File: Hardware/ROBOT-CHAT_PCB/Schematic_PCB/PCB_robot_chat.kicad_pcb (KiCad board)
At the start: 4 copper layers, 64.5 x 57 mm, 95 parts, among them J1 Conn_01x04, J201 Conn_ST_STDC14, J3 Conn_01x02, J4 Conn_01x02, J5 Conn_01x02, J501 Conn_01x04, J502 Conn_01x04, J503 Conn_01x04, J504 Conn_01x04, J6 Conn_01x02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

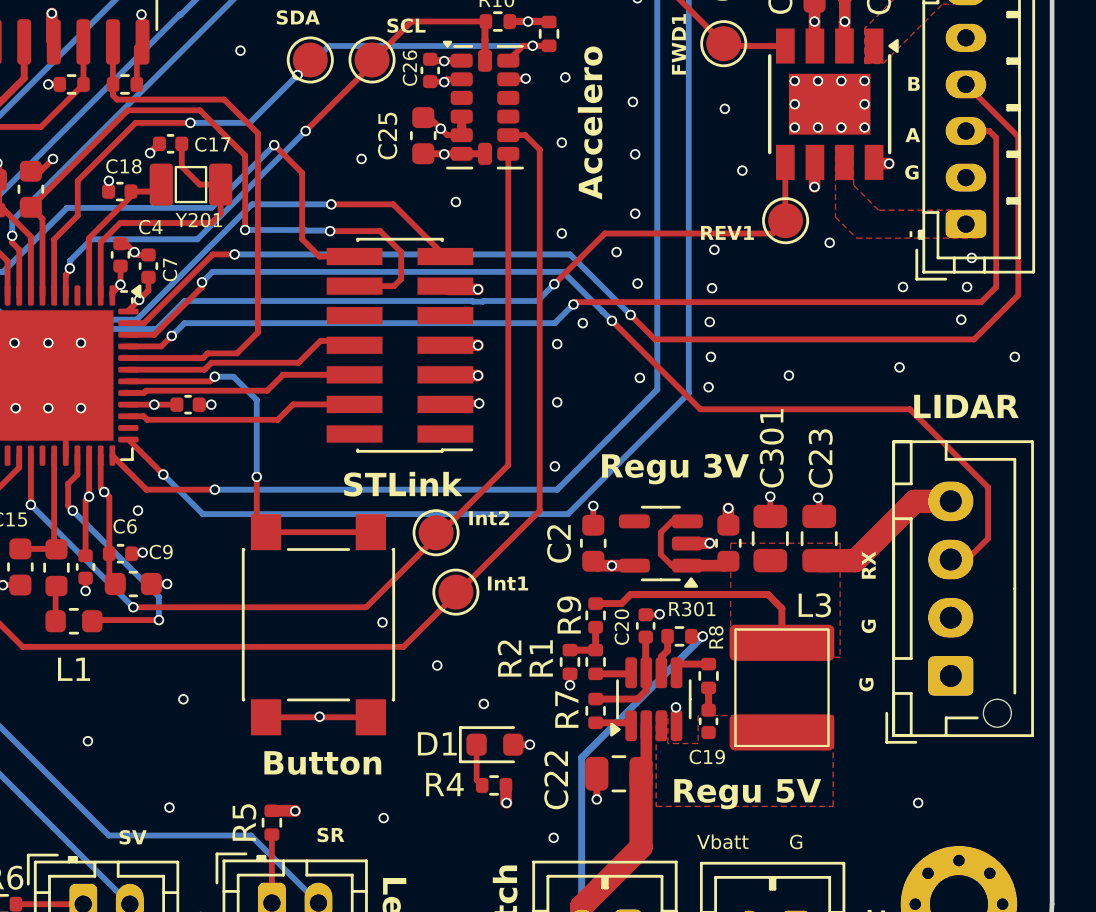
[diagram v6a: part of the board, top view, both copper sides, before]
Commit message: Modified pin M_control for the Lidar, PCV version 7
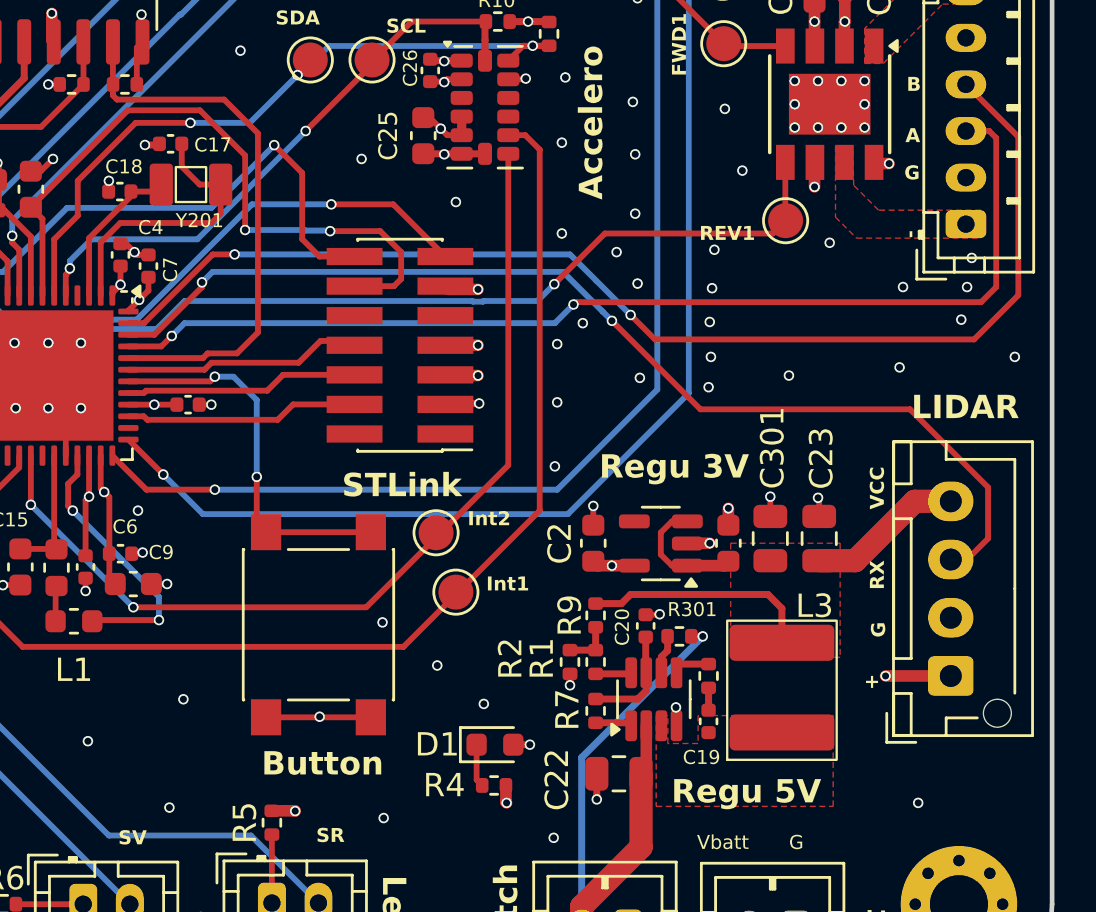
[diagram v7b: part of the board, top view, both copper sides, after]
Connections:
- J1 pad 1: GND -> +3.3V
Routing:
- net +3.3V: track 47.1 -> 49.9 mm, vias 23 -> 24
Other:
- board text added: "VCC"
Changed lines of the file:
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@@
 		(attr smd)
 		(fp_rect
-			(start -2.425 1.5)
-			(end 2.575 5.5)
+			(start -3.025 1.15)
+			(end 2.95 5.85)
 			(stroke
 				(width 0.1)
@@
 			(remove_unused_layers no)
 			(roundrect_rratio 0.147059)
-			(net 2 "GND")
+			(net 3 "+3.3V")
 			(pinfunction "Pin_1")
 			(pintype "passive")
@@
 		(tags "resistor")
 		(property "Reference" "R8"
-			(at -1.65 -0.35 90)
+			(at -1.35 -0.3 90)
 			(layer "F.SilkS")
+			(hide yes)
 			(effects
 				(font
@@
 		(tags "capacitor")
 		(property "Reference" "C19"
-			(at 1.55 0.05 180)
+			(at 1.55 0.3 180)
 			(layer "F.SilkS")
 			(effects
@@
 		)
 	)
-	(gr_text "G"
-		(at 158.4 72.9 90)
-		(layer "F.SilkS")
-		(effects
-			(font
-				(size 0.6 0.6)
-				(thickness 0.15)
-				(bold yes)
-			)
-			(justify left bottom)
-		)
-	)
 	(gr_text "B"
 		(at 159.75 47.15 0)
@@
 		)
 	)
+	(gr_text "VCC"
+		(at 158.85 65.05 90)
+		(layer "F.SilkS")
+		(effects
+			(font
+				(size 0.6 0.6)
+				(thickness 0.15)
+				(bold yes)
+			)
+			(justify left bottom)
+		)
+	)
 	(gr_text "TOF2"
 		(at 116.3 40.2 90)
@@
 	)
 	(gr_text "RX"
-		(at 158.5 68.1 90)
+		(at 158.85 68.5 90)
 		(layer "F.SilkS")
 		(effects
@@
 	)
 	(gr_text "G"
-		(at 158.5 70.4 90)
+		(at 158.9 70.55 90)
 		(layer "F.SilkS")
 		(effects
@@
 		)
 	)
+	(gr_text "+\n"
+		(at 158.6 72.8 90)
+		(layer "F.SilkS")
+		(effects
+			(font
+				(size 0.6 0.6)
+				(thickness 0.15)
+				(bold yes)
+			)
+			(justify left bottom)
+		)
+	)
 	(gr_text "FWD2\n"
 		(at 138.45 39.45 0)
@@
 	)
 	(segment
+		(start 127.62 49.4)
+		(end 127.05 49.4)
+		(width 0.3)
+		(layer "F.Cu")
+		(net 2)
+	)
+	(segment
 		(start 126.48 66.95)
 		(end 126.9 66.95)
@@
 	)
 	(segment
-		(start 127.67 49.35)
-		(end 127.27 49.75)
-		(width 0.3)
-		(layer "F.Cu")
-		(net 2)
-	)
-	(segment
 		(start 133.49 77.99)
 		(end 133.5 78)
@@
 		(net 2)
 	)
+	(segment
+		(start 127.67 49.35)
+		(end 127.62 49.4)
+		(width 0.3)
+		(layer "F.Cu")
+		(net 2)
+	)
 	(via
 		(at 109.85 60.3)
@@
 	)
 	(via
-		(at 127.27 49.75)
+		(at 127.05 49.4)
 		(size 0.45)
 		(drill 0.3)
@@
 	)
 	(segment
+		(start 161.65 72.2)
+		(end 158.85 72.2)
+		(width 0.5)
+		(layer "F.Cu")
+		(net 3)
+	)
+	(segment
 		(start 126.3375 56.55)
 		(end 126.3375 56.5125)
@@
 		(size 0.45)
 		(drill 0.3)
+		(layers "F.Cu" "B.Cu")
+		(net 3)
+	)
+	(via
+		(at 158.85 72.2)
+		(size 0.45)
+		(drill 0.3)

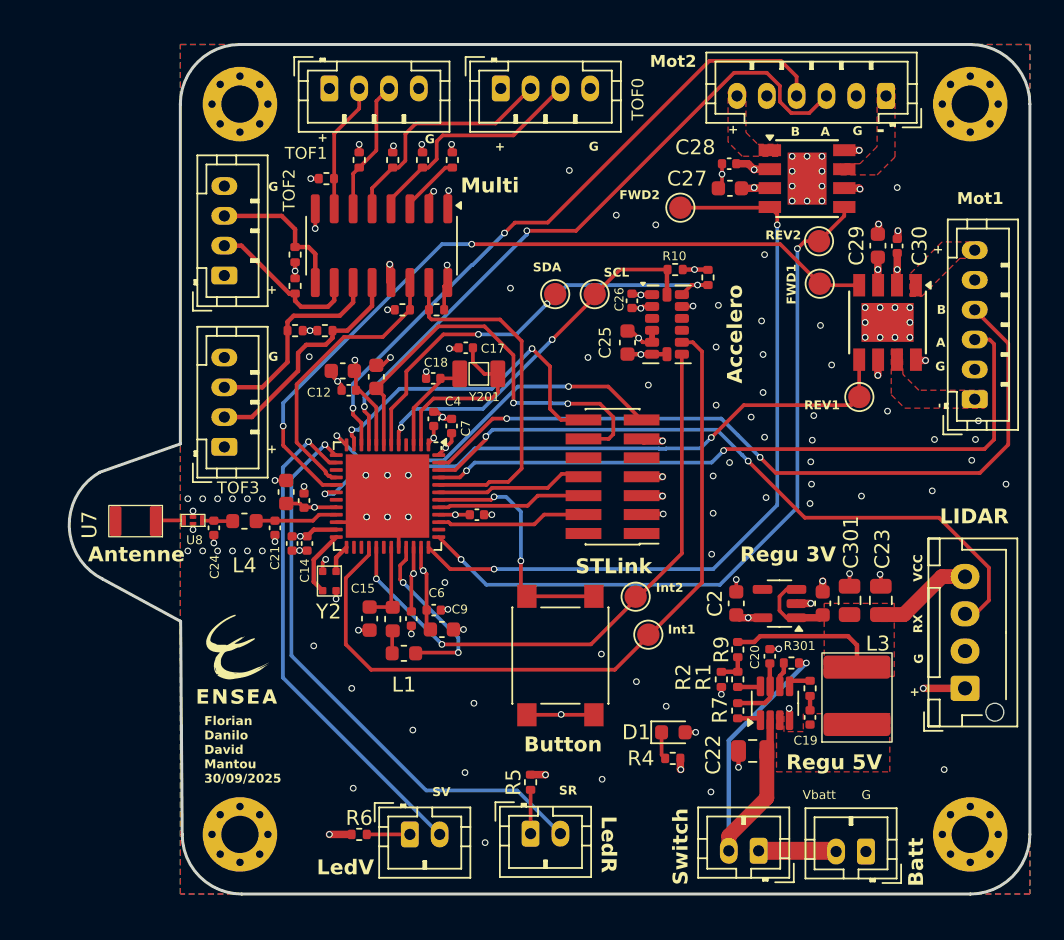
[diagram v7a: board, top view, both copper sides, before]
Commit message: Deleted antenna space btw signals and change R2 value
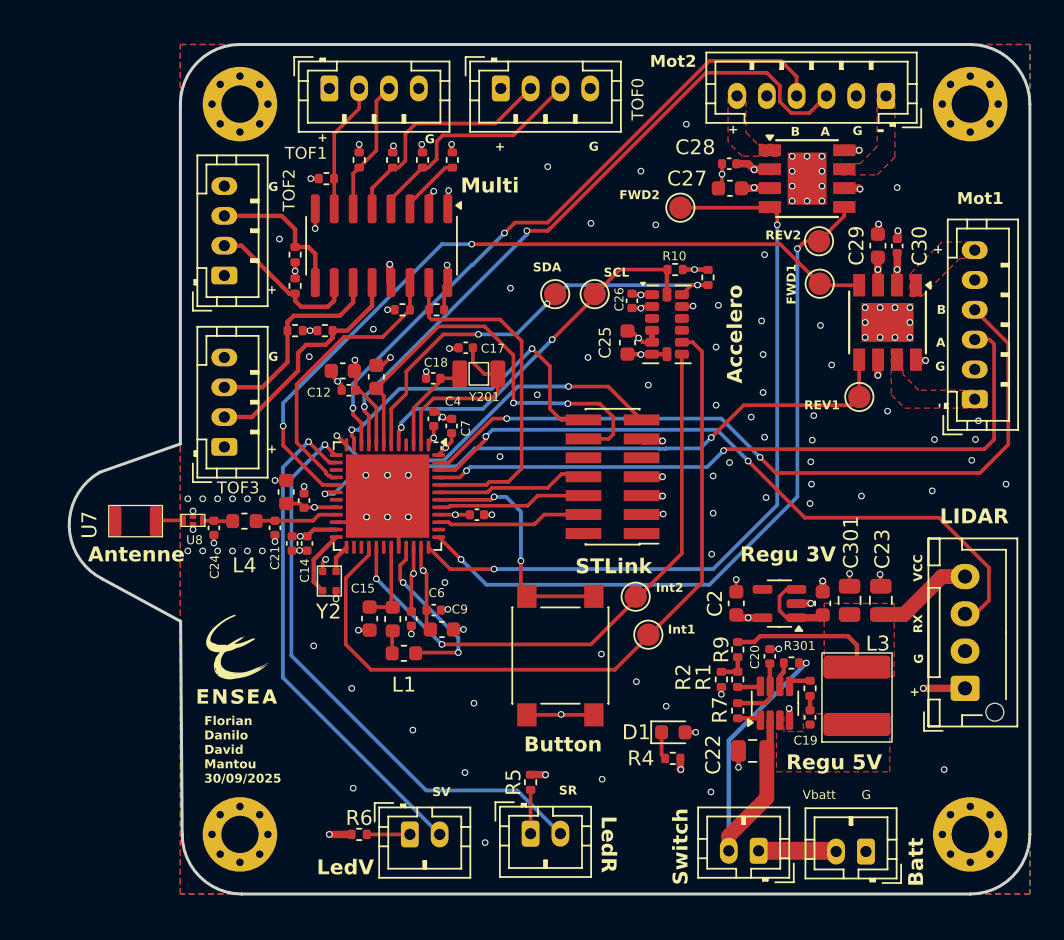
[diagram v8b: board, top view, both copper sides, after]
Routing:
- net GND: vias 136 -> 142
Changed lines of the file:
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@@
 	)
 	(via
+		(at 139.9 37.5)
+		(size 0.45)
+		(drill 0.3)
+		(layers "F.Cu" "B.Cu")
+		(free yes)
+		(net 2)
+	)
+	(via
 		(at 162.55 54.25)
 		(size 0.45)
@@
 	)
 	(via
+		(at 130.45 56.65)
+		(size 0.45)
+		(drill 0.3)
+		(layers "F.Cu" "B.Cu")
+		(free yes)
+		(net 2)
+	)
+	(via
 		(at 126.75 65.1)
 		(size 0.45)
@@
 	)
 	(via
+		(at 121.95 48.1)
+		(size 0.45)
+		(drill 0.3)
+		(layers "F.Cu" "B.Cu")
+		(free yes)
+		(net 2)
+	)
+	(via
 		(at 157.95 47.65)
 		(size 0.45)
@@
 	)
 	(via
+		(at 142.95 34.35)
+		(size 0.45)
+		(drill 0.3)
+		(layers "F.Cu" "B.Cu")
+		(free yes)
+		(net 2)
+	)
+	(via
+		(at 115.65 42.05)
+		(size 0.45)
+		(drill 0.3)
+		(layers "F.Cu" "B.Cu")
+		(free yes)
+		(net 2)
+	)
+	(via
 		(at 114.5 59.48)
 		(size 0.45)
@@
 	)
 	(via
-		(at 138.25 40.45)
+		(at 136.55 41)
 		(size 0.45)
 		(drill 0.3)
@@
 	)
 	(via
-		(at 135.1 37.45)
+		(at 133.65 37.2)
 		(size 0.45)
 		(drill 0.3)
@@
 	)
 	(via
+		(at 132.95 52.5)
+		(size 0.45)
+		(drill 0.3)
+		(layers "F.Cu" "B.Cu")
+		(free yes)
+		(net 2)
+	)
+	(via
 		(at 159.6 55.5)
 		(size 0.45)
@@
 	)
 	(segment
-		(start 146.425 55.225)
-		(end 147.9 56.7)
+		(start 145.3 54.1)
+		(end 130.9 54.1)
 		(width 0.25)
 		(layer "B.Cu")
@@
 	)
 	(segment
-		(start 146.425 55.225)
+		(start 147.9 56.7)
 		(end 145.3 54.1)
 		(width 0.25)
@@
 	)
 	(segment
-		(start 145.3 54.1)
-		(end 130.9 54.1)
-		(width 0.25)
-		(layer "B.Cu")
-		(net 30)
-	)
-	(segment
 		(start 163.3 48.8)
 		(end 163.6 49.1)
@@
 	)
 	(segment
-		(start 128.749 57.051)
+		(start 128.45 57.35)
 		(end 128.2 57.6)
 		(width 0.25)
@@
 	)
 	(segment
-		(start 145.45 56.25)
-		(end 144.649 57.051)
+		(start 144.35 57.35)
+		(end 128.45 57.35)
 		(width 0.25)
 		(layer "B.Cu")
@@
 	)
 	(segment
-		(start 144.649 57.051)
-		(end 128.749 57.051)
+		(start 145.45 56.25)
+		(end 144.35 57.35)
 		(width 0.25)
 		(layer "B.Cu")
@@
 	)
 	(segment
-		(start 121.35 53.6)
-		(end 121.65 53.9)
+		(start 132.25 41.5)
+		(end 133.65 41.5)
 		(width 0.25)
 		(layer "F.Cu")
@@
 	)
 	(segment
-		(start 135.55 41.5)
-		(end 146.15 30.9)
+		(start 149.987149 33.601)
+		(end 151.199 33.601)
 		(width 0.25)
 		(layer "F.Cu")
@@
 	)
 	(segment
-		(start 121.35 53.3)
-		(end 121.35 53.6)
+		(start 133.65 41.5)
+		(end 133.799 41.351)
 		(width 0.25)
 		(layer "F.Cu")
@@
 	)
 	(segment
-		(start 148.35 30.9)
-		(end 149.226 31.776)
+		(start 151.199 33.601)
+		(end 152.35 32.45)
 		(width 0.25)
 		(layer "F.Cu")
@@
 	)
 	(segment
-		(start 121.65 53.9)
-		(end 121.65 55.8625)
+		(start 121.35 53.6)
+		(end 121.65 53.9)
 		(width 0.25)
 		(layer "F.Cu")
@@
 	)
 	(segment
-		(start 149.226 32.839851)
-		(end 149.987149 33.601)
+		(start 121.35 53.3)
+		(end 121.35 53.6)
 		(width 0.25)
 		(layer "F.Cu")
@@
 	)
 	(segment
-		(start 146.15 30.9)
-		(end 148.35 30.9)
+		(start 149.226 31.776)
+		(end 149.226 32.839851)
 		(width 0.25)
 		(layer "F.Cu")
@@
 	)
 	(segment
-		(start 151.199 33.601)
-		(end 152.35 32.45)
+		(start 121.65 53.9)
+		(end 121.65 55.8625)
 		(width 0.25)
 		(layer "F.Cu")
@@
 	)
 	(segment
-		(start 132.25 41.5)
-		(end 135.55 41.5)
+		(start 133.8161 41.351)
+		(end 144.2671 30.9)
 		(width 0.25)
 		(layer "F.Cu")
@@
 	)
 	(segment
-		(start 149.987149 33.601)
-		(end 151.199 33.601)
+		(start 148.35 30.9)
+		(end 149.226 31.776)
 		(width 0.25)
 		(layer "F.Cu")
@@
 	)
 	(segment
-		(start 149.226 31.776)
-		(end 149.226 32.839851)
+		(start 144.2671 30.9)
+		(end 148.35 30.9)
+		(width 0.25)
+		(layer "F.Cu")
+		(net 37)
+	)
+	(segment
+		(start 149.226 32.839851)
+		(end 149.987149 33.601)
+		(width 0.25)
+		(layer "F.Cu")
+		(net 37)
+	)
+	(segment
+		(start 133.799 41.351)
+		(end 133.8161 41.351)
 		(width 0.25)
 		(layer "F.Cu")
@@
 	(segment
 		(start 129.5375 65.25)
-		(end 145.206123 65.25)
+		(end 144.5 65.25)
 		(width 0.25)
 		(layer "B.Cu")
@@
 	)
 	(segment
-		(start 127.8375 63.55)
-		(end 129.5375 65.25)
+		(start 150.4 59.35)
+		(end 150.4 42.7)
 		(width 0.25)
 		(layer "B.Cu")
@@
 	)
 	(segment
-		(start 145.206123 65.25)
-		(end 150.4 60.056123)
+		(start 127.8375 63.55)
+		(end 129.5375 65.25)
 		(width 0.25)
 		(layer "B.Cu")
@@
 	)
 	(segment
-		(start 150.4 60.056123)
-		(end 150.4 42.7)
+		(start 144.5 65.25)
+		(end 150.4 59.35)
 		(width 0.25)
 		(layer "B.Cu")
